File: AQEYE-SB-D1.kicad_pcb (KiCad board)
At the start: 2 copper layers, 80 x 30 mm, 111 parts, among them J1 GPIO15, J10 ZH06_PicoBlade, J11 DHT20, J12 AGS02MA, J13 +3.3V, J14 MB_PINS, J15 MB_CONNECTOR, J16 GND, J17 USB_D+, J18 USB_D-, J19 +5V, J2 DHT20_PAD, J20 GND, J21 SGP40-D-R4_CONN, J22 SCD40-D-R2_CONN, J23 STEMMA-QT, J3 AGS02MA_PAD, J4 GPIO18, J5 ESP_RXD0, J6 ESP_TXD0, J7 I2C_SDA, J8 I2C_SCL, J9 ZH06_Pin, U1 SCD40-D-R2, U2 SGP40-D-R4, U3 AP22804AW5, U4 AP22804AW5

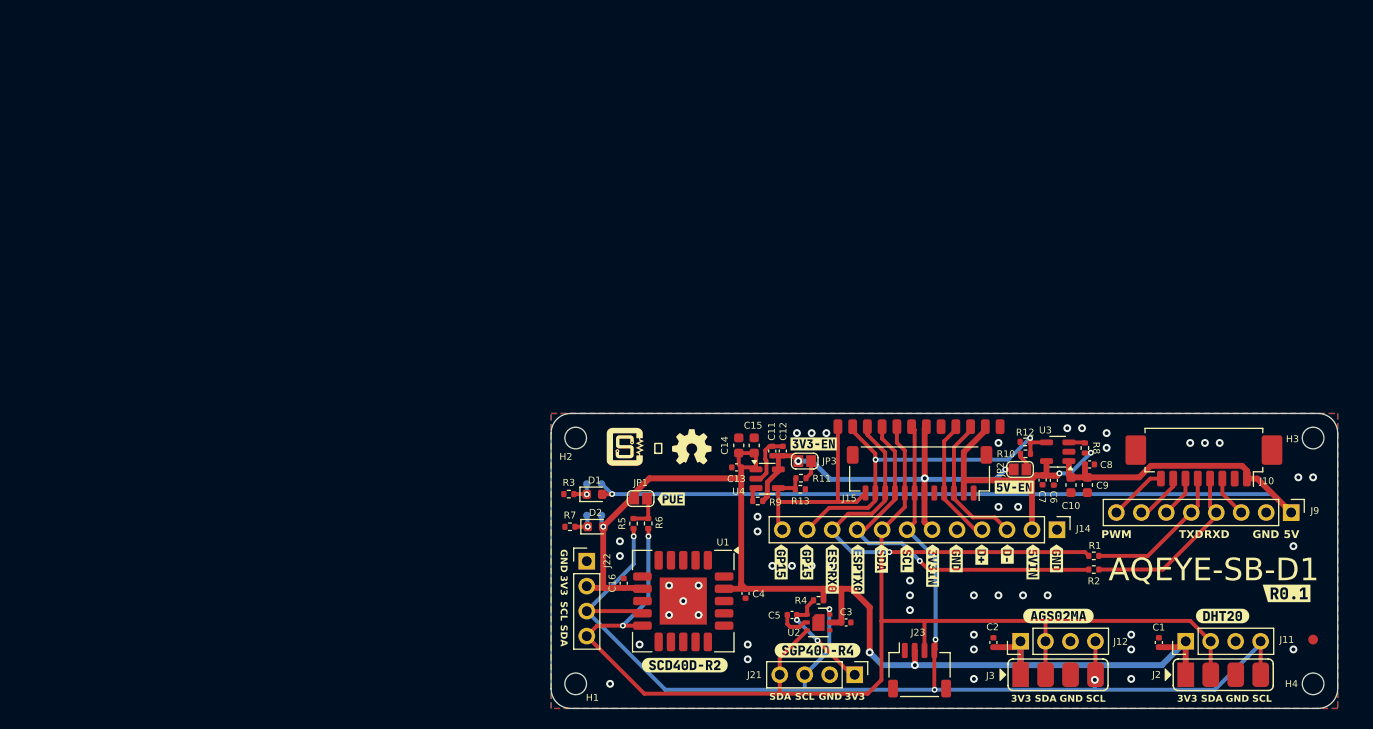
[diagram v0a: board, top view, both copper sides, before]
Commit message: Generated manufacturing files
- Schematic
  - Updated BoM.
  - Assigned all MPNs.
  - Added `Group by MPN-DNP` preset.
- PCB
  - Imported all changes to the PCB.
  - Cleaned up the Fab layers.
  - Added CIRCUITSTATE logo and GitHub link to schematic.
  - Applied teardrops.
  - Added board stackup table and characteristics.
  - DRC passes.
- Added KiExport configuration.
- Added Git scripts.
- Generated manufacturing files.
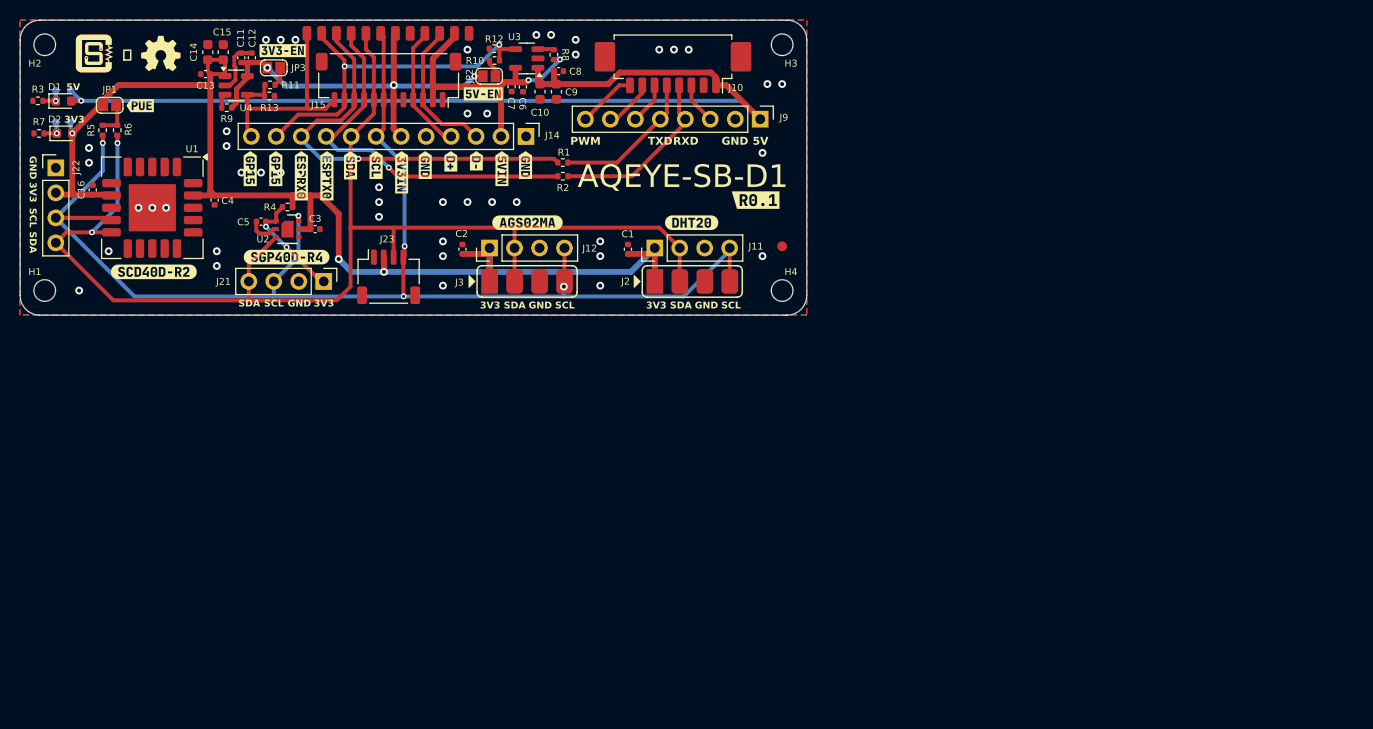
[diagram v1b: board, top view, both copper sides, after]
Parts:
- C12, C3, C5, C7: value 1uF -> 10uF
- moved kibuzzard-68408D87 67.4 mm to (115.7, 84.9)
- moved G*** 67.2 mm to (124.3, 69.4)
- moved J11 67.2 mm to (174.5, 89.2)
- moved J12 67.2 mm to (157.7, 89.2)
- moved REF** 67.2 mm to (121.3, 69.5)
- moved kibuzzard-68408D87 67.2 mm to (123.6, 91.6)
- moved C1 67.2 mm to (171.8, 89.3)
- moved C10 67.2 mm to (162.9, 73.3)
- moved C11 67.2 mm to (132.5, 69.8)
- moved C12 67.2 mm to (133.6, 69.8)
- moved C13 67.2 mm to (128.9, 71.5)
- moved C14 67.2 mm to (129.1, 69.3)
- moved C15 67.2 mm to (130.7, 69.3)
- moved C16 67.2 mm to (117.4, 83.3)
- moved C2 67.2 mm to (155.0, 89.3)
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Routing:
- net GND: vias 47 -> 45
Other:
- board text added: "0"
- board text added: "0 mm"
- board text added: "0.01 mm"
- board text added: "0.02"
- board text added: "0.035 mm"
- board text added: "0.2000 mm / 0.2000 mm"
- board text added: "0.3000 mm"
- board text added: "1"
- board text added: "1.51 mm"
- board text added: "1.6000 mm"
- board text added: "2"
- board text added: "3.3"
- board text added: "4.5"
- board text added: "80.0000 mm x 30.0000 mm"
- board text added: "B.Cu"
- board text added: "B.Mask"
- board text added: "B.Paste"
- board text added: "B.Silkscreen"
- board text added: "BOARD CHARACTERISTICS"
- board text added: "Board Thickness:"
- board text added: "Board overall dimensions:"
- board text added: "Bottom Silk Screen"
- board text added: "Bottom Solder Mask"
- board text added: "Bottom Solder Paste"
- board text added: "Castellated pads:"
- board text added: "Color"
- board text added: "Copper Finish:"
- board text added: "Copper Layer Count:"
- board text added: "Dielectric"
- board text added: "Edge card connectors:"
- board text added: "Epsilon R"
- board text added: "F.Cu"
- board text added: "F.Mask"
- board text added: "F.Paste"
- board text added: "F.Silkscreen"
- board text added: "FR4"
- board text added: "Impedance Control:"
- board text added: "Layer Name"
- board text added: "Loss Tangent"
- board text added: "Material"
- board text added: "Min hole diameter:"
- board text added: "Min track/spacing:"
- board text added: "No"
- board text added: "None"
- board text added: "Not specified"
- board text added: "Plated Board Edge:"
- board text added: "Thickness (mm)"
- board text added: "Top Silk Screen"
- board text added: "Top Solder Mask"
- board text added: "Top Solder Paste"
- board text added: "Type"
- board text added: "copper"
- board text added: "core"

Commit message: Added 5V boost converter
- Schematic
  - Realized that the main board can not supply 5V when the USB is not connected.
  - Added a `TPS61023` 5V boost converter to generate 5V from the 3.3V input.
  - Removed the 5V load switch since the 5V output can not be controlled via the boost converter.
  - The 5V converter enabled by default with a GPIO control.
  - Added `LM66100DCKR` single-channel ideal diode to connect the VBUS to the 5V rail.
  - Reset the annotations.
  - Updated the BoM.
- PCB
  - Imported all changes to the PCB.
  - Placement and routing completed.
  - DRC passes.
  - Updated Fab layers.
  - Updated KiExport configuration.
    - New STEP and VRML options are added.
- Generated manufacturing files.
- No version change.
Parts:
- removed the C10 at (162.9, 73.3)
- removed the C6 at (161.1, 72.8)
- removed the JP2 at (157.7, 71.7)
- removed the R10 at (158.2, 70.1)
- removed the R8 at (164.3, 69.5)
- removed kibuzzard-68408F46: G***, kibuzzard-68408F46
- added L1: 1uH, Inductor_SMD:L_Changjiang_FNR6020S, F.Cu at (161.9, 73.1)
- added R13: 10K, Resistor_SMD:R_0402_1005Metric, F.Cu at (164.1, 80.0)
- added R14: 732K, Resistor_SMD:R_0402_1005Metric, F.Cu at (159.4, 67.1)
- added R15: 100K, Resistor_SMD:R_0402_1005Metric, F.Cu at (157.7, 67.6)
- added U4: TPS61023, Package_TO_SOT_SMD:SOT-563, F.Cu at (161.7, 68.4)
- C7: value 10uF -> 22uF; footprint Capacitor_SMD:C_0402_1005Metric -> Capacitor_SMD:C_0603_1608Metric
- C8: value 0.1uF -> 22uF; footprint Capacitor_SMD:C_0402_1005Metric -> Capacitor_SMD:C_0603_1608Metric
- U3: value AP22804AW5 -> LM66100DCKR; footprint Package_TO_SOT_SMD:SOT-23-5 -> Package_TO_SOT_SMD:SOT-363_SC-70-6
- moved U3 8.60 mm to (164.7, 77.9), turned to 0 degrees
- moved C9 5.29 mm to (166.1, 68.2)
- moved C7 3.63 mm to (156.8, 71.0), turned to 180 degrees
- moved C8 2.99 mm to (164.4, 68.2), turned to -90 degrees
- moved R12 1.72 mm to (156.6, 69.6), turned to 180 degrees
- moved R2 1.40 mm to (165.1, 83.3)
- moved R1 1.10 mm to (165.1, 81.6)
- renumbered C11 to C10, C12 to C11, C13 to C12, C14 to C13, C15 to C14, C16 to C3, C3 to C4, C4 to C5, C5 to C6, J13 to J11, J14 to J12, J15 to J13, J11 to J14, J12 to J15, J23 to J24, JP3 to JP2, R9 to R10, R13 to R16, R5 to R3, R6 to R4, R4 to R5, R3 to R8, R7 to R9, U4 to U5
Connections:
- C7 pad 1: +5V_IN -> +3.3V_IN
- R12 pad 1: GND -> /GPIO18
- R12 pad 2: /GPIO18 -> +3.3V_IN
- U3 pad 1: +5V -> +5V_IN
- U3 pad 4: /GPIO18 -> unconnected-(U3-NC-Pad4)
- U3 pad 5: +5V_IN -> GND
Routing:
- net +5V: track 101.0 -> 113.4 mm
- net +3.3V_IN: track 42.2 -> 52.9 mm, vias 3 -> 7
- net +5V_IN: track 29.3 -> 22.7 mm, vias 2 -> 0
- net GND: track 8.86 -> 15.0 mm, vias 45 -> 52
- net Net-(U4-FB): track 0.00 -> 3.72 mm
- net Net-(JP2-A) (its old number): track 1.84 -> 0.00 mm
- net Net-(J10-Pin_4): track 18.3 -> 19.0 mm
- net Net-(J10-Pin_5): track 15.0 -> 15.5 mm
- added copper zone on B.Cu, net +3.3V_IN
- added copper zone on F.Cu, net +3.3V_IN
- added copper zone on F.Cu, net +5V
- added copper zone on F.Cu, net Net-(U4-SW)
